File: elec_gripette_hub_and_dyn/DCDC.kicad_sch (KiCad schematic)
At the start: 33 parts, among them J2 JST EH 2, J7 Pogo-pin, J8 Pogo-pin, Q2 SI2312CDS-T1-GE3, U6 MP2338, U7 AP63205, U8 LM5050-1

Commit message: [update] sch reviewed by Claude
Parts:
- removed R17: 51k, Resistor_SMD:R_0402_1005Metric, symbol Device:R_Small
- J7, J8: value Pogo-pin -> Pogo-pin 2A; footprint LCSC_parts_lib:SMD_BD2.0-L2.0-W2.0_C9900001905 -> LCSC_parts_lib:CONN-TH_YZ08415060P-02_pogo; LCSC Part C2826547 -> C7471674
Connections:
- net at C16.1, C18.1, C19.1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: now also R16.2; no longer R16.1
- net at U6.1 (PG): now also R16.1; no longer R16.2
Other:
- moved on the sheet: R16, U6

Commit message: [update] Gripette hub routed
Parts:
- J2: footprint Connector_JST:JST_EH_S2B-EH_1x02_P2.50mm_Horizontal -> Connector_JST:JST_EH_B2B-EH-A_1x02_P2.50mm_Vertical; LCSC Part C514173 -> (none)
- R19, R20, R28: footprint Resistor_SMD:R_0402_1005Metric -> Resistor_SMD:R_0603_1608Metric; LCSC Part C17168 -> (none)
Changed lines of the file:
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@@
 			)
 		)
-		(property "Footprint" "Resistor_SMD:R_0402_1005Metric"
+		(property "Footprint" "Resistor_SMD:R_0603_1608Metric"
 			(at 173.99 59.69 0)
 			(effects
@@
 			)
 		)
-		(property "LCSC Part" "C17168"
+		(property "LCSC Part" ""
 			(at 173.99 59.69 90)
 			(effects
@@
 			)
 		)
-		(property "Footprint" "Resistor_SMD:R_0402_1005Metric"
+		(property "Footprint" "Resistor_SMD:R_0603_1608Metric"
 			(at 207.01 45.72 0)
 			(effects
@@
 			)
 		)
-		(property "LCSC Part" "C17168"
+		(property "LCSC Part" ""
 			(at 207.01 45.72 90)
 			(effects
@@
 			)
 		)
-		(property "Footprint" "Resistor_SMD:R_0402_1005Metric"
+		(property "Footprint" "Resistor_SMD:R_0603_1608Metric"
 			(at 173.99 55.88 0)
 			(effects
@@
 			)
 		)
-		(property "LCSC Part" "C17168"
+		(property "LCSC Part" ""
 			(at 173.99 55.88 90)
 			(effects
@@
 			)
 		)
-		(property "Footprint" "Connector_JST:JST_EH_S2B-EH_1x02_P2.50mm_Horizontal"
+		(property "Footprint" "Connector_JST:JST_EH_B2B-EH-A_1x02_P2.50mm_Vertical"
 			(at 31.75 45.72 0)
 			(effects
@@
 			)
 		)
-		(property "LCSC Part" "C514173"
+		(property "LCSC Part" ""
 			(at 31.75 45.72 0)
 			(effects

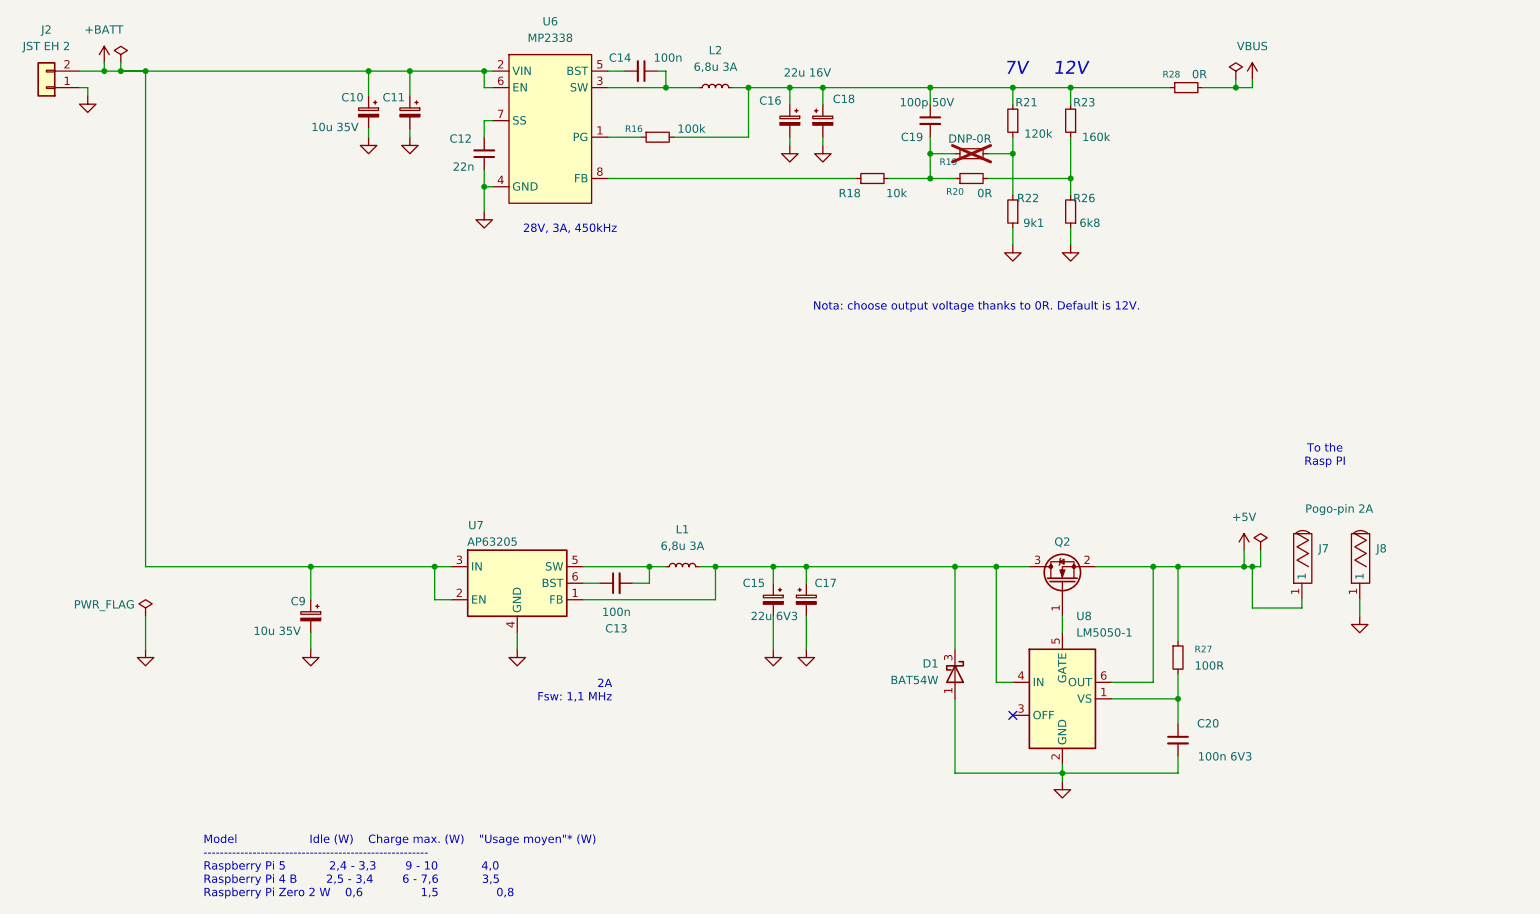
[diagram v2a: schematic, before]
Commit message: [update] Gripette bulkhead ready for production.
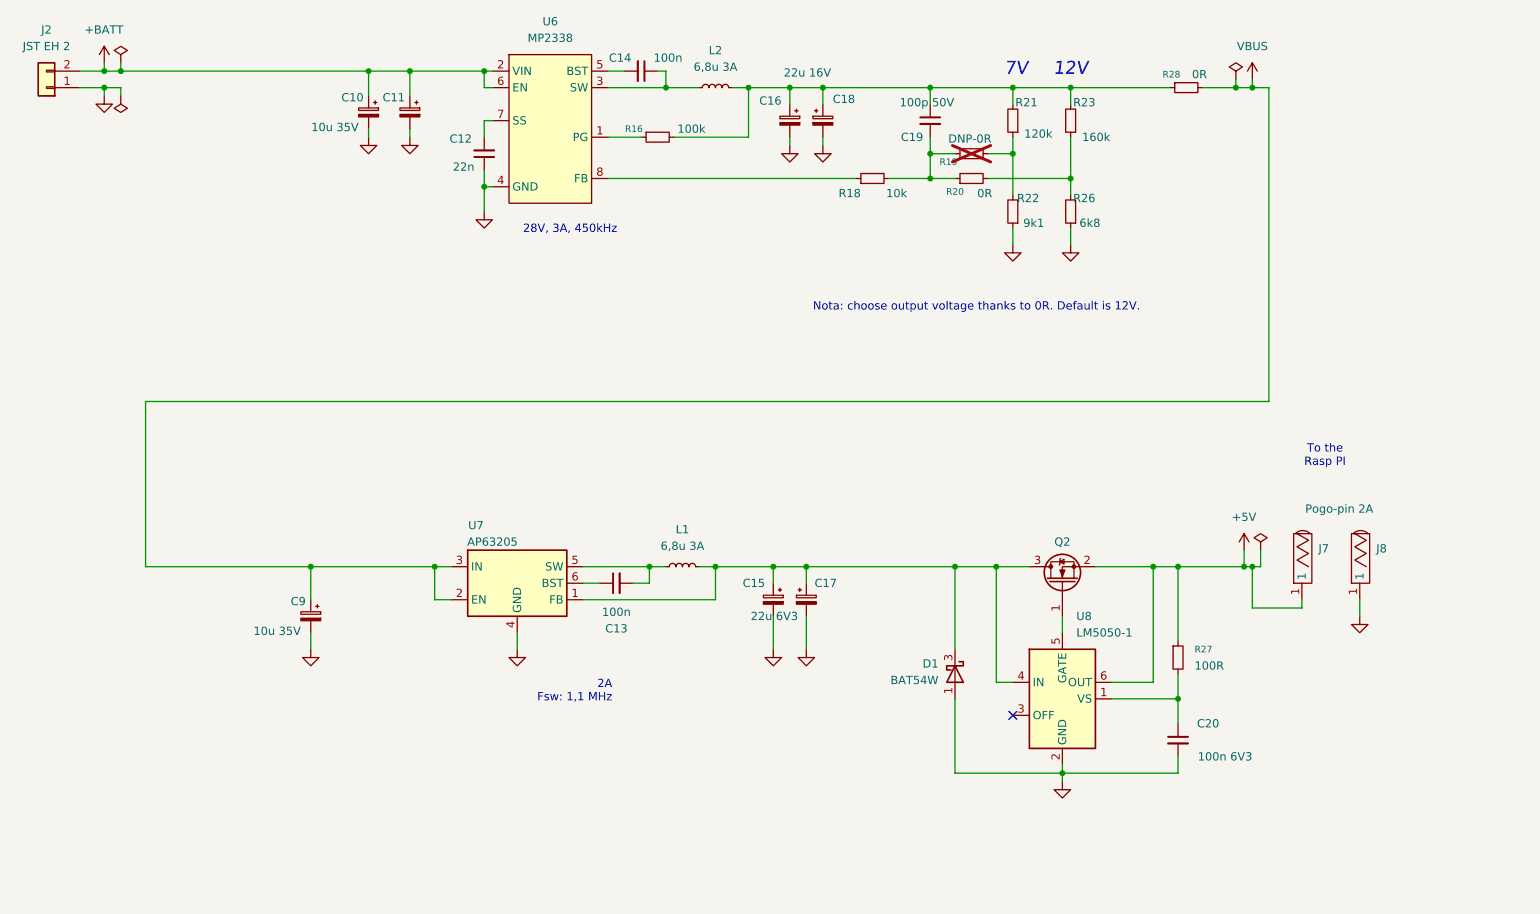
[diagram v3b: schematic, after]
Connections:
- net +BATT: no longer C9.1, U7.2 (EN), U7.3 (IN)
- net VBUS: now also C9.1, U7.2 (EN), U7.3 (IN)
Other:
- note removed: "Model Idle (W) Charge max. (W) "Usage moyen"* (W) ------------------------------------------------------- Raspberry Pi 5 2,4 - 3,3 9 - 10 4,0 Raspberry Pi 4 B 2,5 - 3,4 6 - 7,6 3,5 Raspberry Pi Zero 2 W 0,6 1,5 0,8"
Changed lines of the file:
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@@
 		)
 	)
-	(text "Model					Idle (W)	Charge max. (W)	\"Usage moyen\"* (W)\n-------------------------------------------------------\nRaspberry Pi 5			2,4 - 3,3		9 - 10			4,0\nRaspberry Pi 4 B		2,5 - 3,4		6 - 7,6			3,5\nRaspberry Pi Zero 2 W	0,6				1,5				0,8"
-		(exclude_from_sim no)
-		(at 55.88 165.608 0)
-		(effects
-			(font
-				(size 1.27 1.27)
-			)
-			(justify left)
-		)
-	)
 	(junction
-		(at 46.99 43.18)
+		(at 171.45 119.38)
 		(diameter 0)
 		(color 0 0 0 0)
 	)
 	(junction
-		(at 171.45 119.38)
+		(at 217.17 45.72)
 		(diameter 0)
 		(color 0 0 0 0)
@@
 	)
 	(junction
+		(at 40.64 45.72)
+		(diameter 0)
+		(color 0 0 0 0)
+	)
+	(junction
 		(at 189.23 59.69)
 		(diameter 0)
@@
 	(wire
 		(pts
-			(xy 43.18 43.18) (xy 46.99 43.18)
+			(xy 43.18 43.18) (xy 81.28 43.18)
 		)
 		(stroke
@@
 	(wire
 		(pts
-			(xy 43.18 43.18) (xy 46.99 43.18)
-		)
-		(stroke
-			(width 0)
-			(type default)
-		)
-	)
-	(wire
-		(pts
 			(xy 177.8 119.38) (xy 182.88 119.38)
 		)
@@
 	(wire
 		(pts
+			(xy 43.18 46.99) (xy 43.18 45.72)
+		)
+		(stroke
+			(width 0)
+			(type default)
+		)
+	)
+	(wire
+		(pts
 			(xy 195.58 137.16) (xy 201.93 137.16)
 		)
@@
 	(wire
 		(pts
-			(xy 46.99 127) (xy 46.99 132.08)
+			(xy 43.18 45.72) (xy 40.64 45.72)
 		)
 		(stroke
-			(width 0.5)
+			(width 0)
 			(type default)
 		)
@@
 	(wire
 		(pts
-			(xy 46.99 43.18) (xy 46.99 119.38)
+			(xy 46.99 93.98) (xy 219.71 93.98)
 		)
 		(stroke
@@
 	(wire
 		(pts
-			(xy 38.1 45.72) (xy 38.1 46.99)
+			(xy 40.64 45.72) (xy 40.64 46.99)
 		)
 		(stroke
@@
 	(wire
 		(pts
-			(xy 46.99 43.18) (xy 81.28 43.18)
-		)
-		(stroke
-			(width 0.5)
-			(type default)
-		)
-	)
-	(wire
-		(pts
 			(xy 127 45.72) (xy 132.08 45.72)
 		)
@@
 	(wire
 		(pts
+			(xy 219.71 45.72) (xy 217.17 45.72)
+		)
+		(stroke
+			(width 0.5)
+			(type default)
+		)
+	)
+	(wire
+		(pts
+			(xy 219.71 93.98) (xy 219.71 45.72)
+		)
+		(stroke
+			(width 0.5)
+			(type default)
+		)
+	)
+	(wire
+		(pts
 			(xy 99.06 64.77) (xy 99.06 60.96)
 		)
@@
 	(wire
 		(pts
+			(xy 46.99 119.38) (xy 46.99 93.98)
+		)
+		(stroke
+			(width 0.5)
+			(type default)
+		)
+	)
+	(wire
+		(pts
 			(xy 214.63 44.45) (xy 214.63 45.72)
 		)
@@
 	(wire
 		(pts
-			(xy 36.83 45.72) (xy 38.1 45.72)
+			(xy 36.83 45.72) (xy 40.64 45.72)
 		)
 		(stroke
@@
 	(symbol
 		(lib_id "power:PWR_FLAG")
-		(at 46.99 127 0)
-		(mirror y)
+		(at 43.18 46.99 0)
+		(mirror x)
 		(unit 1)
 		(exclude_from_sim no)
@@
 		(dnp no)
 		(property "Reference" "#FLG02"
-			(at 46.99 125.095 0)
+			(at 43.18 48.895 0)
 			(effects
 				(font
@@
 		)
 		(property "Value" "PWR_FLAG"
-			(at 40.64 125.222 0)
+			(at 49.53 48.768 0)
 			(effects
 				(font
 					(size 1.27 1.27)
 				)
+				(hide yes)
 			)
 		)
 		(property "Footprint" ""
-			(at 46.99 127 0)
+			(at 43.18 46.99 0)
 			(effects
 				(font
@@
 		)
 		(property "Datasheet" "~"
-			(at 46.99 127 0)
+			(at 43.18 46.99 0)
 			(effects
 				(font
@@
 		)
 		(property "Description" ""
-			(at 46.99 127 0)
+			(at 43.18 46.99 0)
 			(effects
 				(font
@@
 	(symbol
 		(lib_id "power:GND")
-		(at 38.1 46.99 0)
+		(at 40.64 46.99 0)
 		(unit 1)
 		(exclude_from_sim no)
@@
 		(fields_autoplaced yes)
 		(property "Reference" "#PWR01"
-			(at 38.1 53.34 0)
+			(at 40.64 53.34 0)
 			(effects
 				(font
@@
 		)
 		(property "Value" "GND"
-			(at 38.1 52.07 0)
+			(at 40.64 52.07 0)
 			(effects
 				(font
@@
 		)
 		(property "Footprint" ""
-			(at 38.1 46.99 0)
+			(at 40.64 46.99 0)
 			(effects
 				(font
@@
 		)
 		(property "Datasheet" ""
-			(at 38.1 46.99 0)
+			(at 40.64 46.99 0)
 			(effects
 				(font
@@
 		)
 		(property "Description" "Power symbol creates a global label with name \"GND\" , ground"
-			(at 38.1 46.99 0)
+			(at 40.64 46.99 0)
 			(effects
 				(font
@@
 					(unit 1)
 				)
-			)
-		)
-	)
-	(symbol
-		(lib_id "power:GND")
-		(at 46.99 132.08 0)
-		(unit 1)
-		(exclude_from_sim no)
-		(in_bom yes)
-		(on_board yes)
-		(dnp no)
-		(fields_autoplaced yes)
-		(property "Reference" "#PWR03"
-			(at 46.99 138.43 0)
-			(effects
-				(font
-					(size 1.27 1.27)
-				)
-				(hide yes)
-			)
-		)
-		(property "Value" "GND"
-			(at 46.99 137.16 0)
-			(effects
-				(font
-					(size 1.27 1.27)
-				)
-				(hide yes)
-			)
-		)
-		(property "Footprint" ""
-			(at 46.99 132.08 0)
-			(effects
-				(font
-					(size 1.27 1.27)
-				)
-				(hide yes)
-			)
-		)
-		(property "Datasheet" ""
-			(at 46.99 132.08 0)
-			(effects
-				(font
-					(size 1.27 1.27)
-				)
-				(hide yes)
-			)
-		)
-		(property "Description" "Power symbol creates a global label with name \"GND\" , ground"
-			(at 46.99 132.08 0)
-			(effects
-				(font
-					(size 1.27 1.27)
-				)
-				(hide yes)
-			)
-		)
-		(pin "1"
-		)
-		(instances
-			(project "elec_gripette_hub_and_dyn"
-				(path "/bc05f5da-608c-4912-90e4-36b13d989976/75f3f8ec-6d80-4862-afd6-8e1e61b07901"
-					(reference "#PWR03")
-					(unit 1)
-				)

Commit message: [uptate] Gripette hub ok for JLC
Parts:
- C16, C18: FT Rotation Offset (none) -> 180
- J2: FT Rotation Offset 180 -> (none); LCSC Part (none) -> C160262
- R19: value DNP-0R -> DNP - 0R
- R20, R28: LCSC Part (none) -> C21189
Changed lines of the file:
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@@
 	(title_block
 		(title "Grippette - USB hub and Dynamixel device")
-		(date "2026-04-07")
+		(date "2026-04-16")
 		(rev "A1")
 		(company "Pollen Robotics/HF")
@@
 			)
 		)
-		(property "LCSC Part" ""
+		(property "LCSC Part" "C21189"
 			(at 173.99 59.69 90)
 			(effects
@@
 			)
 		)
-		(property "LCSC Part" ""
+		(property "LCSC Part" "C21189"
 			(at 207.01 45.72 90)
 			(effects
@@
 			)
 		)
+		(property "FT Rotation Offset" "180"
+			(at 146.05 50.8 0)
+			(effects
+				(font
+					(size 1.27 1.27)
+				)
+				(hide yes)
+			)
+		)
 		(pin "1"
 		)
@@
 			)
 		)
-		(property "Value" "DNP-0R"
+		(property "Value" "DNP - 0R"
 			(at 173.736 53.594 90)
 			(effects
@@
 			)
 		)
-		(property "LCSC Part" ""
+		(property "LCSC Part" "C160262"
 			(at 31.75 45.72 0)
 			(effects
@@
 			)
 		)
-		(property "FT Rotation Offset" "180"
+		(property "FT Rotation Offset" ""
 			(at 31.75 45.72 0)
 			(effects
@@
 			(at 151.13 50.8 0)
 			(effects
+				(font
+					(size 1.27 1.27)
+				)
+				(hide yes)
+			)
+		)
+		(property "FT Rotation Offset" "180"
+			(at 151.13 50.8 0)
+			(effects

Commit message: [update] Added error to gripette, going to B1
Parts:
- R19: value DNP - 0R -> DNP-0R
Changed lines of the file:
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@@
 		(dnp no)
 		(property "Reference" "R21"
-			(at 184.15 48.006 0)
+			(at 184.912 47.752 0)
 			(effects
 				(font
@@
 		(dnp no)
 		(property "Reference" "R22"
-			(at 184.404 62.738 0)
+			(at 185.166 61.976 0)
 			(effects
 				(font
@@
 			)
 		)
-		(property "Value" "DNP - 0R"
+		(property "Value" "DNP-0R"
 			(at 173.736 53.594 90)
 			(effects
@@
 		(dnp no)
 		(property "Reference" "R23"
-			(at 193.04 48.006 0)
+			(at 193.548 47.752 0)
 			(effects
 				(font
@@
 		(dnp no)
 		(property "Reference" "R26"
-			(at 193.04 62.738 0)
+			(at 193.802 61.976 0)
 			(effects
 				(font

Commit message: [update] SCH B1-RC1
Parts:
- removed R23: 160k, Resistor_SMD:R_0402_1005Metric, symbol Device:R_Small
- removed U6: MP2338, LCSC_parts_lib:SOT-583-8_L2.1-W1.2-P0.50-LS1.6-BR, symbol Library_Pollen:MP2338
- added D10: D_Schottky 3A, Diode_SMD:D_SMA, symbol Device:D_Schottky
- added R30, R31: DNP, Resistor_SMD:R_0603_1608Metric, symbol Device:R_Small
- added R32: 243k, Resistor_SMD:R_0402_1005Metric, symbol Device:R_Small
- added U9: TPS54560BDDA, Package_SO:Texas_R-PDSO-G8_EP2.95x4.9mm_Mask2.4x3.1mm_ThermalVias, symbol Regulator_Switching:TPS54560BDDA
- C12: value 22n -> 4n7; LCSC Part C1532 -> C1518204
- C19: value 100p 50V -> 47p; LCSC Part C106200 -> C1567
- J7: value Pogo-pin 2A -> Pogo-pin 2A 4mm
- L2: symbol Device:L_Small -> Device:L_Iron
- R18: value 10k -> 16k9; LCSC Part C25744 -> C25858
- R21: value 120k -> 62k; LCSC Part C2909314 -> C2909375
- R22: value 9k1 -> 8k2; LCSC Part C2909390 -> C25924
- R26: value 6k8 -> 7k5; LCSC Part C2906876 -> C25918
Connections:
- net +BATT: now also C9.1, U7.2 (EN), U7.3 (IN), R30.1, U9.2 (VIN)
- net GND: now also C12.2, C19.2, D10.2 (A), R31.1, R32.1, U9.7 (GND), U9.9 (GND); no longer C12.1
- net VBUS: no longer C9.1, U7.2 (EN), U7.3 (IN)
- net at C16.1, C18.1, L2.1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: now also R16.1; no longer C19.1, R16.2
- net at C14.1, L2.2: now also D10.1 (K), U9.8 (SW)
- net at C14.2: now also U9.1 (BOOT)
- net at R18.1: now also C19.1, U9.6 (COMP)
- net at R19.1, R20.1: now also U9.5 (FB); no longer C19.2, R18.2
- net at R20.2, R26.2: now also R16.2
- new net: C12.1, R18.2
- new net: R32.2, U9.4 (RT/CLK)
- new net: R30.2, R31.2, U9.3 (EN)
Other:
- note added: "60V, 5A, 400kHz"
- note removed: "28V, 3A, 450kHz"
- moved on the sheet: C10, C11, C14, C16, C18, R16, R19, R20, R21, R22, R26, R28

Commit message: [update] SCH + PCB B1-RC1
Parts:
- J8: value Pogo-pin 2A -> Pogo-pin 2A 4mm
- R30, R31: footprint Resistor_SMD:R_0603_1608Metric -> Resistor_SMD:R_0402_1005Metric
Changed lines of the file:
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@@
 			)
 		)
-		(property "Value" "Pogo-pin 2A"
+		(property "Value" "Pogo-pin 2A 4mm"
 			(at 236.22 119.1432 90)
 			(effects
@@
 			)
 		)
-		(property "Footprint" "Resistor_SMD:R_0603_1608Metric"
+		(property "Footprint" "Resistor_SMD:R_0402_1005Metric"
 			(at 85.09 48.26 0)
 			(effects
@@
 			)
 		)
-		(property "Footprint" "Resistor_SMD:R_0603_1608Metric"
+		(property "Footprint" "Resistor_SMD:R_0402_1005Metric"
 			(at 85.09 50.8 0)
 			(effects

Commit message: [update] review by Claude. Corrections, RC2
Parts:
- added C27: 3,3u 35V, Capacitor_SMD:C_0805_2012Metric, symbol Device:C_Small
- U9: LCSC Part (none) -> C1850354
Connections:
- net +5V: now also Q2.3 (D); no longer Q2.2 (S)
- net +BATT: now also C27.1
- net GND: now also C27.2
- net at C15.1, C17.1, D1.3 (K)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: now also Q2.2 (S); no longer Q2.3 (D)
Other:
- moved on the sheet: C10, C11, C12, C13, C14, C15, C16, C17, C18, C19, C20, C9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
